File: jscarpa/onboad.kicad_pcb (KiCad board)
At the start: 2 copper layers, 55.6 x 42.3 mm, 11 parts, among them J1 Conn_01x02_Socket, J2 Conn_01x02_Socket, U1 ACS711xLCTR-12AB, U2 mcp6546-e/p

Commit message: Onboarding: Flipped threw hole components.
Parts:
- D1, J1, J2, R1, R2, R3, R4, U2: moved to B.Cu
- moved J2 38.9 mm to (128.7, 95.6), turned to 90 degrees
- moved J1 38.3 mm to (128.8, 84.3)
- moved R1 36.7 mm to (92.2, 103.0), turned to 0 degrees
- moved R3 26.7 mm to (91.0, 85.2), turned to -90 degrees
- moved C1 25.5 mm to (116.6, 97.9), turned to 90 degrees
- moved R4 21.7 mm to (96.8, 85.2), turned to -90 degrees
- moved U1 18.6 mm to (119.1, 93.0), turned to 180 degrees
- moved C2 17.3 mm to (114.2, 87.1)
- moved U2 10.4 mm to (110.4, 95.7)
- moved D1 8.58 mm to (108.2, 84.1), turned to 90 degrees
- moved R2 5.87 mm to (109.9, 103.0), turned to 0 degrees
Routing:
- net GND: track 38.0 -> 0.00 mm
- net +3V3: track 82.2 -> 70.8 mm
- net Current-: track 9.40 -> 0.00 mm
- net Current+: track 8.84 -> 0.00 mm
- net Net-(U2-VIN+): track 20.3 -> 12.5 mm
- net Net-(D1-A): track 6.74 -> 0.00 mm
- net Net-(D1-K): track 21.5 -> 16.0 mm
- net Net-(U1-VIOUT): track 9.48 -> 10.8 mm
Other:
- board size 55.6 x 42.3 mm -> 51.6 x 35.3 mm

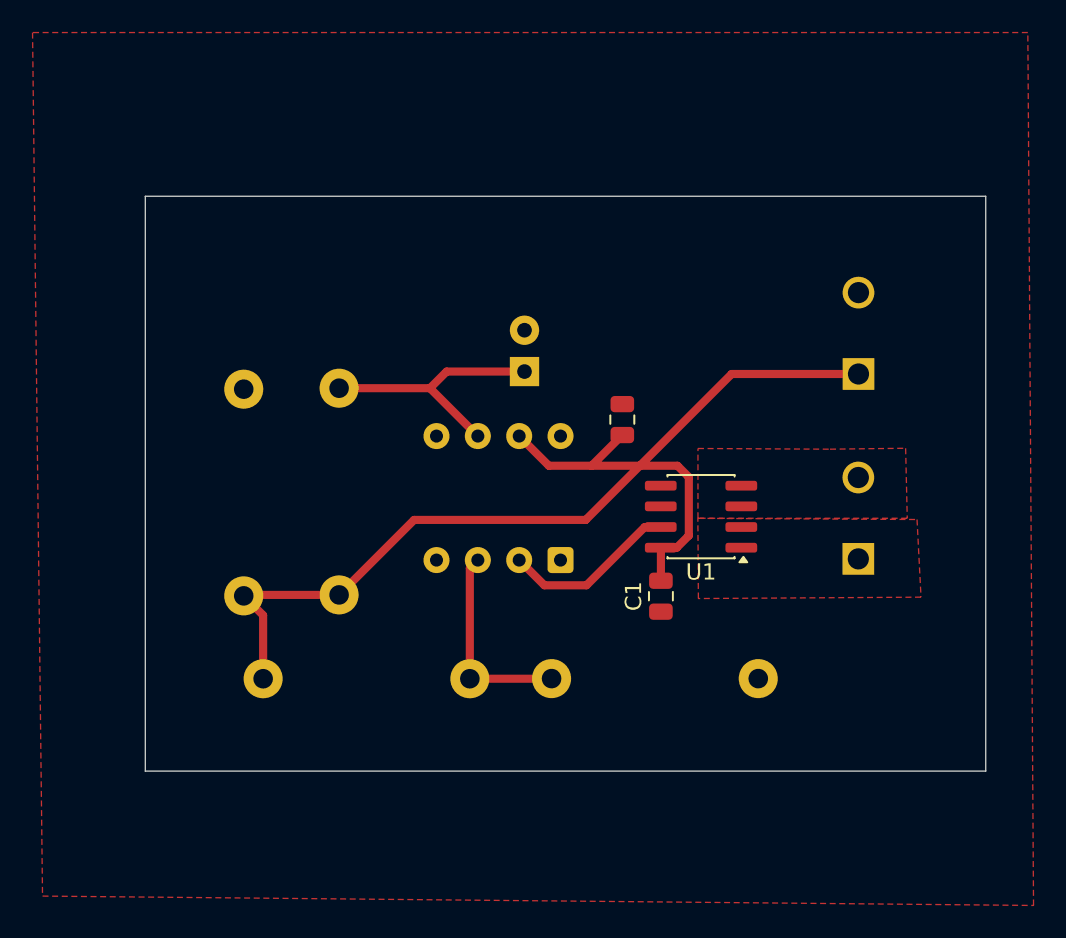
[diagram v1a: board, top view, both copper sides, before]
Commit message: Onboarding: Fixed footprint and symbol library directories.
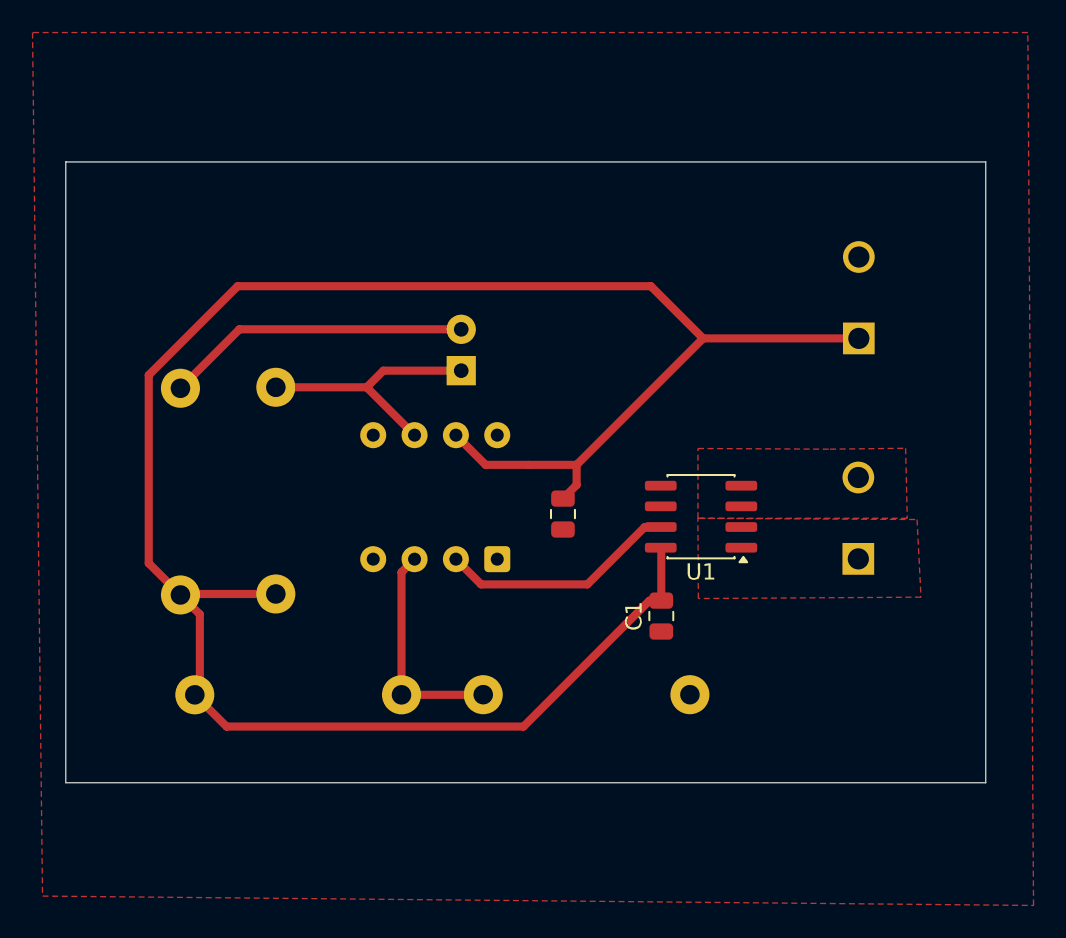
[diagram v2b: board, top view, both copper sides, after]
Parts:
- moved C2 6.86 mm to (110.6, 92.9), turned to 90 degrees
- moved R1 4.31 mm to (88.0, 104.0)
- moved R2 4.31 mm to (105.7, 104.0)
- moved U2 3.89 mm to (106.6, 95.7)
- moved D1 3.89 mm to (104.3, 84.1)
- moved R4 3.89 mm to (92.9, 85.1)
- moved R3 3.89 mm to (87.1, 85.2)
- moved J1 2.19 mm to (128.8, 82.1)
- moved C1 1.22 mm to (116.6, 99.2)
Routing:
- net +3V3: track 70.8 -> 130.5 mm
- net Net-(D1-A): track 0.00 -> 18.8 mm
- net Net-(U1-VIOUT): track 10.8 -> 14.7 mm
- net Net-(U2-VIN+): track 12.5 -> 13.7 mm
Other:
- board size 51.6 x 35.3 mm -> 56.5 x 38.1 mm
